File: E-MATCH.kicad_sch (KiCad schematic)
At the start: 23 parts, among them IC1 NCV81071BZR2G, IC2 NCV81071BZR2G, J1 691210910002, J2 691210910002, J3 691210910002, J4 691210910002, J5 DC Jack, Q1 AOSP36326C, Q2 AOSP36326C, Q3 AOSP36326C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

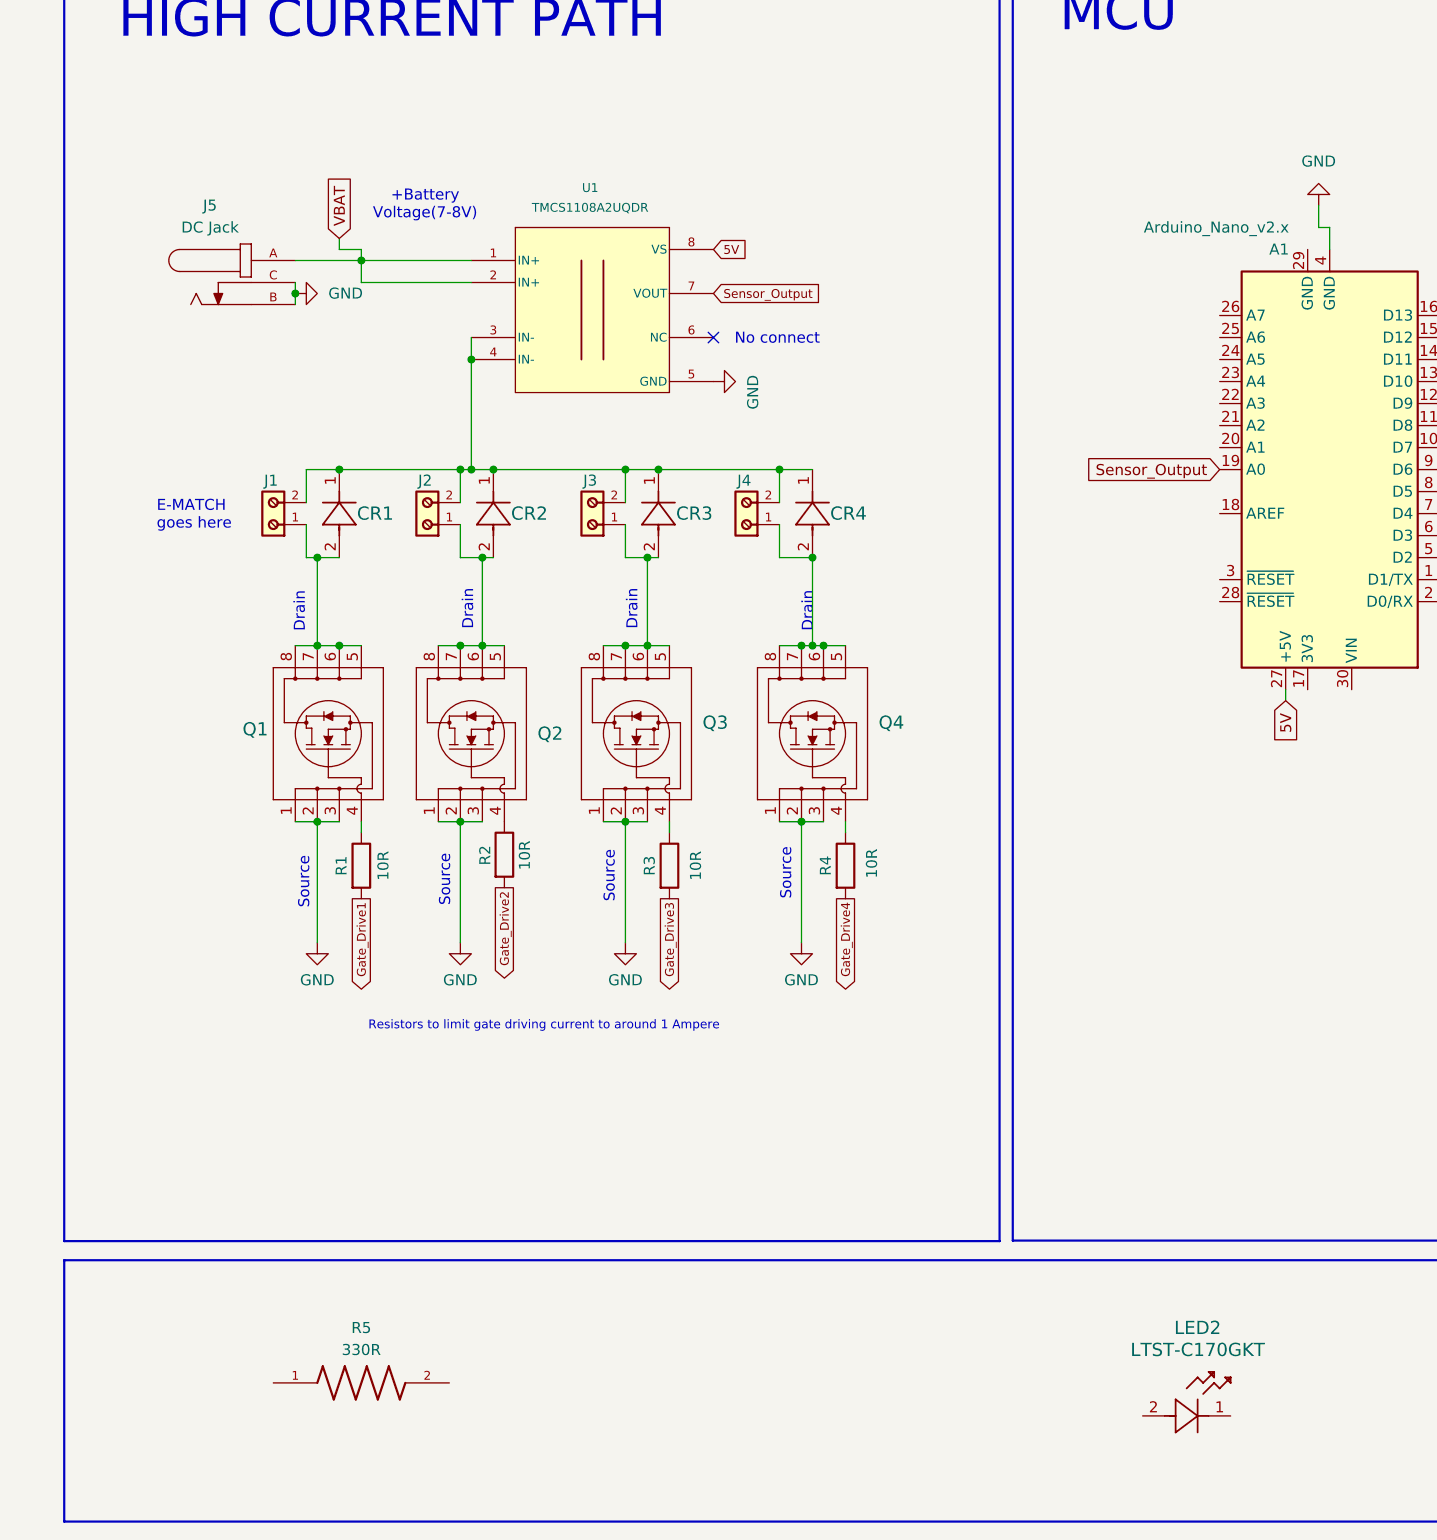
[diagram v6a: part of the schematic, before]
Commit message: added the Led and resistor to 5V
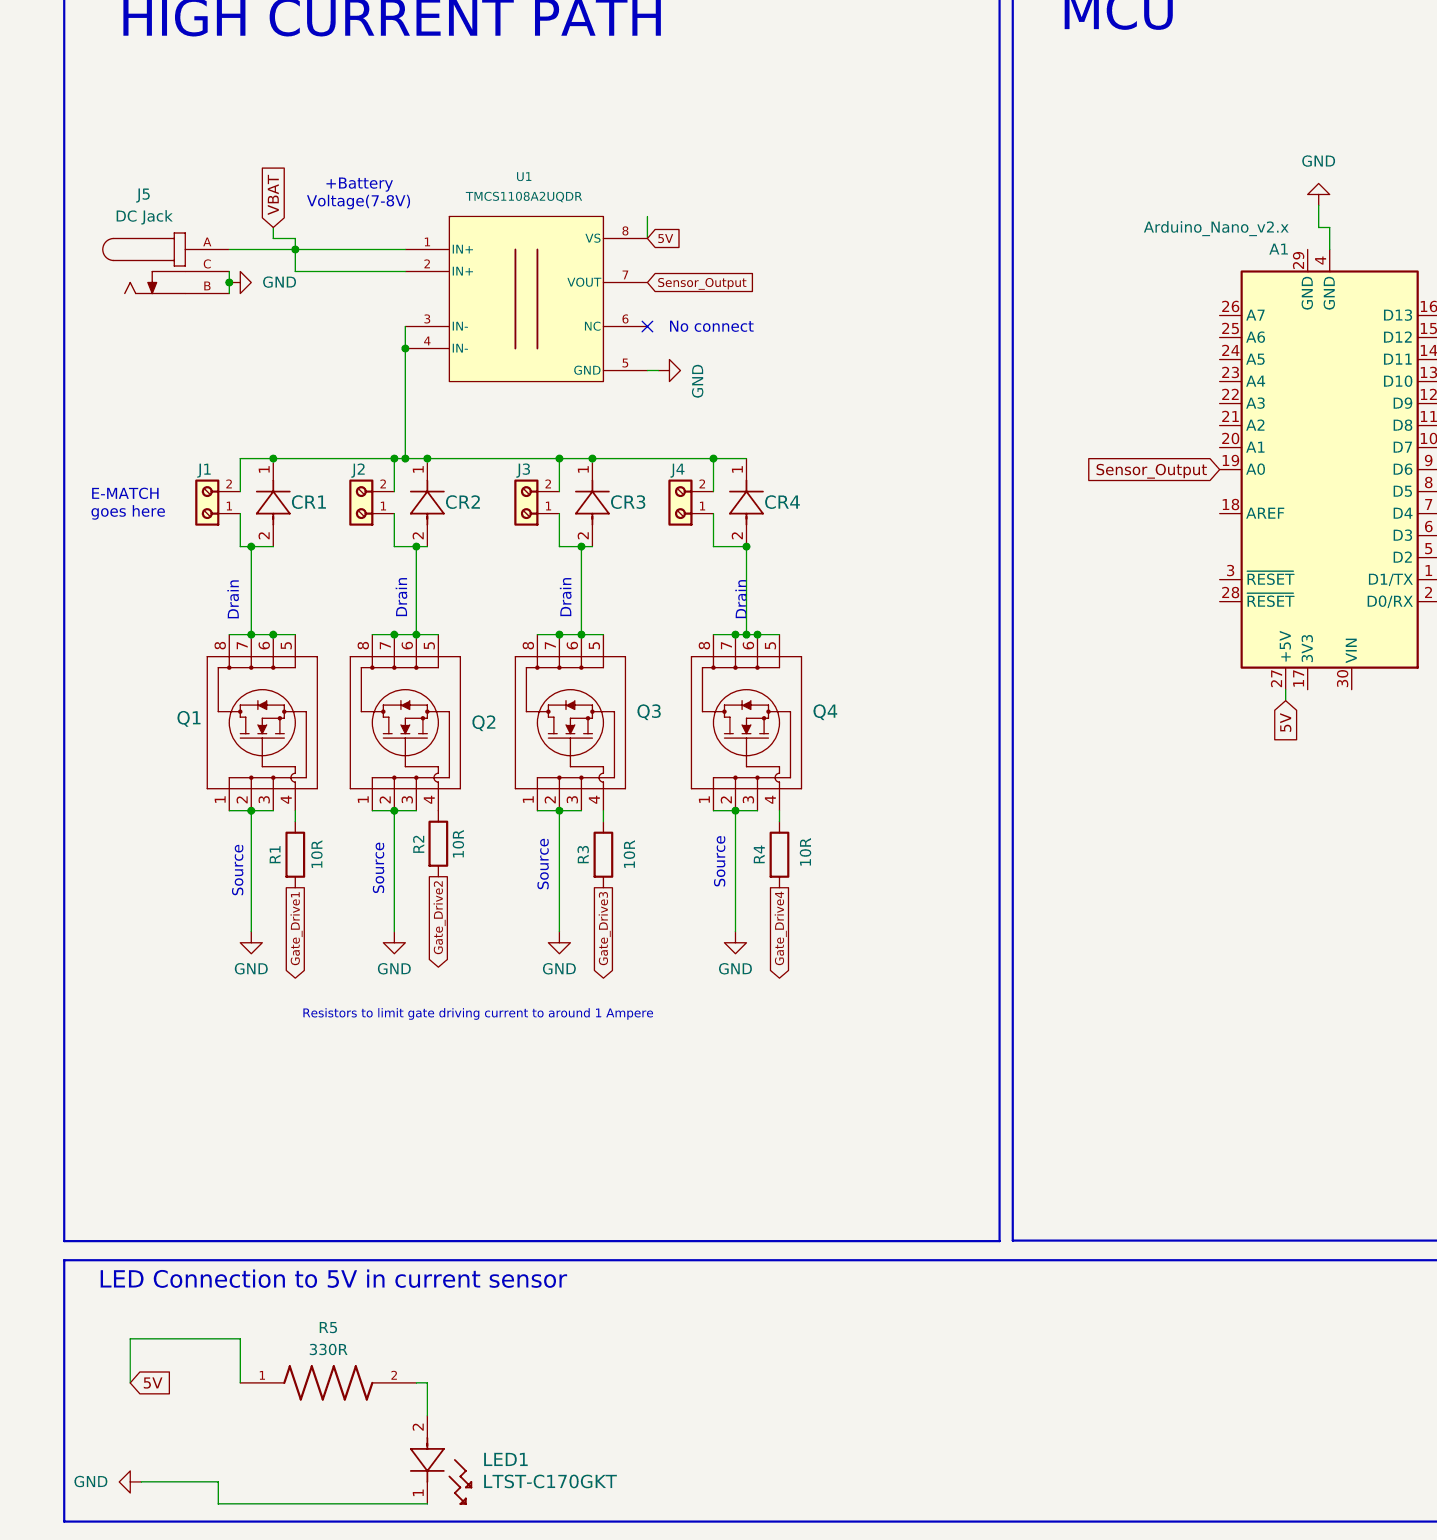
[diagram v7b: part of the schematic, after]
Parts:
- removed LED2: LTST-C170GKT, LED_LTST-C170GKT_LTO, symbol LTST-C170GKT:LTST-C170GKT
- added LED1: LTST-C170GKT, LED_LTST-C170GKT_LTO, symbol LTST-C170GKT:LTST-C170GKT
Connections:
- net 5V: now also R5.1
- net GND: now also LED1.1
- net at R5.2: now also LED1.2
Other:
- note added: "LED Connection to 5V in current sensor"
- moved on the sheet: CR1, CR2, CR3, CR4, J1, J2, J3, J4, J5, Q1, Q2, Q3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

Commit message: schematic cleanup
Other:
- note added: "LED INDICATORS"
- note removed: "LED Connection to 5V in current sensor"
- moved on the sheet: LED1, R5
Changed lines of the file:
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@@
 		)
 	)
-	(text "LED Connection to 5V in current sensor"
+	(text "LED INDICATORS"
 		(exclude_from_sim no)
-		(at 44.958 168.656 0)
+		(at 42.418 173.482 0)
 		(effects
 			(font
-				(size 2 2)
+				(size 4.318 4.318)
 			)
 		)
@@
 	(wire
 		(pts
-			(xy 34.29 175.26) (xy 34.29 180.34)
-		)
-		(stroke
-			(width 0)
-			(type default)
-		)
-	)
-	(wire
-		(pts
 			(xy 54.61 93.98) (xy 54.61 83.82)
 		)
@@
 	(wire
 		(pts
-			(xy 31.75 191.77) (xy 22.86 191.77)
-		)
-		(stroke
-			(width 0)
-			(type default)
-		)
-	)
-	(wire
-		(pts
 			(xy 88.9 73.66) (xy 92.71 73.66)
 		)
@@
 	(wire
 		(pts
-			(xy 55.88 180.34) (xy 55.88 184.15)
-		)
-		(stroke
-			(width 0)
-			(type default)
-		)
-	)
-	(wire
-		(pts
-			(xy 54.61 180.34) (xy 55.88 180.34)
+			(xy 111.76 181.61) (xy 113.03 181.61)
 		)
 		(stroke
@@
 	(wire
 		(pts
-			(xy 21.59 175.26) (xy 34.29 175.26)
-		)
-		(stroke
-			(width 0)
-			(type default)
-		)
-	)
-	(wire
-		(pts
 			(xy 71.12 83.82) (xy 73.66 83.82)
 		)
@@
 	(wire
 		(pts
-			(xy 55.88 194.31) (xy 31.75 194.31)
-		)
-		(stroke
-			(width 0)
-			(type default)
-		)
-	)
-	(wire
-		(pts
 			(xy 73.66 93.98) (xy 73.66 83.82)
 		)
@@
 	(wire
 		(pts
-			(xy 21.59 180.34) (xy 21.59 175.26)
-		)
-		(stroke
-			(width 0)
-			(type default)
-		)
-	)
-	(wire
-		(pts
 			(xy 40.64 48.26) (xy 40.64 49.53)
 		)
@@
 	(wire
 		(pts
-			(xy 31.75 194.31) (xy 31.75 191.77)
-		)
-		(stroke
-			(width 0)
-			(type default)
-		)
-	)
-	(wire
-		(pts
 			(xy 256.54 53.34) (xy 255.27 53.34)
 		)
@@
 	(global_label "5V"
 		(shape input)
-		(at 21.59 180.34 0)
+		(at 91.44 181.61 180)
 		(fields_autoplaced yes)
 		(effects
@@
 				(size 1.27 1.27)
 			)
-			(justify left)
+			(justify right)
 		)
 		(property "Intersheetrefs" "${INTERSHEET_REFS}"
-			(at 26.8733 180.34 0)
+			(at 86.1567 181.61 0)
 			(effects
 				(font
 					(size 1.27 1.27)
 				)
-				(justify left)
+				(justify right)
 				(hide yes)
 			)
@@
 	(symbol
 		(lib_id "power:GND")
-		(at 22.86 191.77 270)
+		(at 123.19 181.61 90)
 		(unit 1)
 		(exclude_from_sim no)
@@
 		(fields_autoplaced yes)
 		(property "Reference" "#PWR08"
-			(at 16.51 191.77 0)
+			(at 129.54 181.61 0)
 			(effects
 				(font
@@
 		)
 		(property "Value" "GND"
-			(at 19.05 191.7699 90)
+			(at 127 181.6099 90)
 			(effects
 				(font
@@
 		)
 		(property "Footprint" ""
-			(at 22.86 191.77 0)
+			(at 123.19 181.61 0)
 			(effects
 				(font
@@
 		)
 		(property "Datasheet" ""
-			(at 22.86 191.77 0)
+			(at 123.19 181.61 0)
 			(effects
 				(font
@@
 		)
 		(property "Description" "Power symbol creates a global label with name \"GND\" , ground"
-			(at 22.86 191.77 0)
+			(at 123.19 181.61 0)
 			(effects
 				(font
@@
 	(symbol
 		(lib_id "RC0603JR-07330RL:RC0603JR-07330RL")
-		(at 44.45 180.34 0)
+		(at 101.6 181.61 0)
 		(unit 1)
 		(exclude_from_sim no)
@@
 		(fields_autoplaced yes)
 		(property "Reference" "R5"
-			(at 44.45 173.99 0)
+			(at 101.6 175.26 0)
 			(effects
 				(font
@@
 		)
 		(property "Value" "330R"
-			(at 44.45 176.53 0)
+			(at 101.6 177.8 0)
 			(effects
 				(font
@@
 		)
 		(property "Footprint" "SMD_RESISTOR:RESC1608X55N"
-			(at 44.45 180.34 0)
+			(at 101.6 181.61 0)
 			(effects
 				(font
@@
 		)
 		(property "Datasheet" ""
-			(at 44.45 180.34 0)
+			(at 101.6 181.61 0)
 			(effects
 				(font
@@
 		)
 		(property "Description" ""
-			(at 44.45 180.34 0)
+			(at 101.6 181.61 0)
 			(effects
 				(font
@@
 		)
 		(property "DigiKey_Part_Number" "311-330GRCT-ND"
-			(at 44.45 180.34 0)
+			(at 101.6 181.61 0)
 			(effects
 				(font
@@
 		)
 		(property "SnapEDA_Link" "https://www.snapeda.com/parts/RC0603JR-07330RL/Yageo/view-part/?ref=snap"
-			(at 44.45 180.34 0)
+			(at 101.6 181.61 0)
 			(effects
 				(font
@@
 		)
 		(property "Description_1" "330 Ohms ±5% 0.1W, 1/10W Chip Resistor 0603 (1608 Metric) Moisture Resistant Thick Film"
-			(at 44.45 180.34 0)
+			(at 101.6 181.61 0)
 			(effects
 				(font
@@
 		)
 		(property "MF" "Yageo"
-			(at 44.45 180.34 0)
+			(at 101.6 181.61 0)
 			(effects
 				(font
@@
 		)
 		(property "Package" "1608 Yageo"
-			(at 44.45 180.34 0)
+			(at 101.6 181.61 0)
 			(effects
 				(font
@@
 		)
 		(property "Check_prices" "https://www.snapeda.com/parts/RC0603JR-07330RL/Yageo/view-part/?ref=eda"
-			(at 44.45 180.34 0)
+			(at 101.6 181.61 0)
 			(effects
 				(font
@@
 		)
 		(property "MP" "RC0603JR-07330RL"
-			(at 44.45 180.34 0)
+			(at 101.6 181.61 0)
 			(effects
 				(font
@@
 	(symbol
 		(lib_id "LTST-C170GKT:LTST-C170GKT")
-		(at 55.88 184.15 270)
+		(at 113.03 181.61 0)
 		(unit 1)
 		(exclude_from_sim no)
@@
 		(fields_autoplaced yes)
 		(property "Reference" "LED1"
-			(at 62.23 189.2299 90)
+			(at 119.38 171.45 0)
 			(effects
 				(font
 					(size 1.524 1.524)
 				)
-				(justify left)
 			)
 		)
 		(property "Value" "LTST-C170GKT"
-			(at 62.23 191.7699 90)
+			(at 119.38 173.99 0)
 			(effects
 				(font
 					(size 1.524 1.524)
 				)
-				(justify left)
 			)
 		)
 		(property "Footprint" "LED_LTST-C170GKT_LTO"
-			(at 55.88 184.15 0)
+			(at 113.03 181.61 0)
 			(effects
 				(font
@@
 		)
 		(property "Datasheet" "LTST-C170GKT"
-			(at 55.88 184.15 0)
+			(at 113.03 181.61 0)
 			(effects
 				(font
@@
 		)
 		(property "Description" ""
-			(at 55.88 184.15 0)
+			(at 113.03 181.61 0)
 			(effects
 				(font
